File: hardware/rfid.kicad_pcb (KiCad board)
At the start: 2 copper layers, 75 x 50 mm, 34 parts, among them P1 CONN_01X02, P2 COMMS, U1 CR95HF

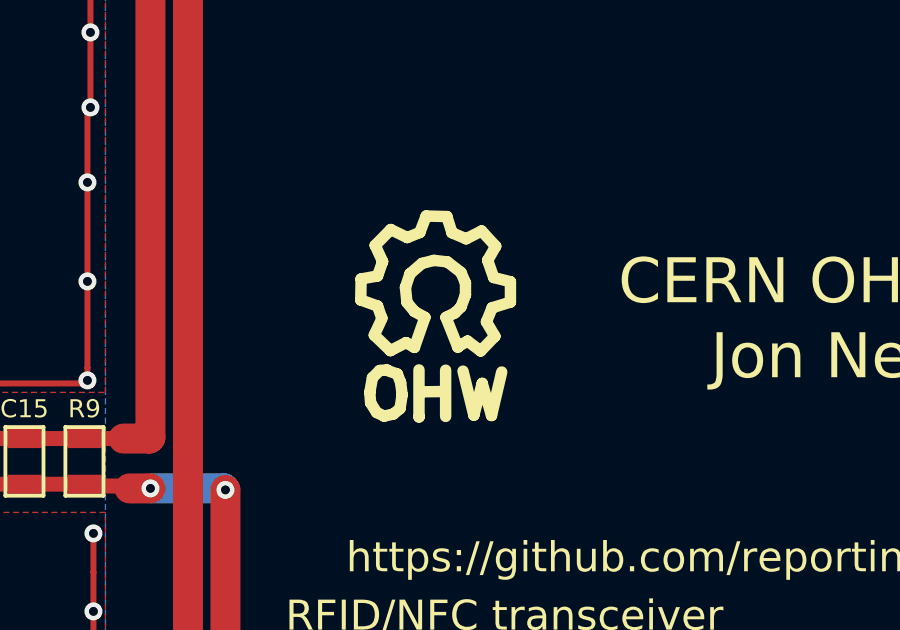
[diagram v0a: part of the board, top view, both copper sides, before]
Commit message: Thought that the correct phrase was OHW when it is actually OSHW. Updated board and gerbers to reflect this.
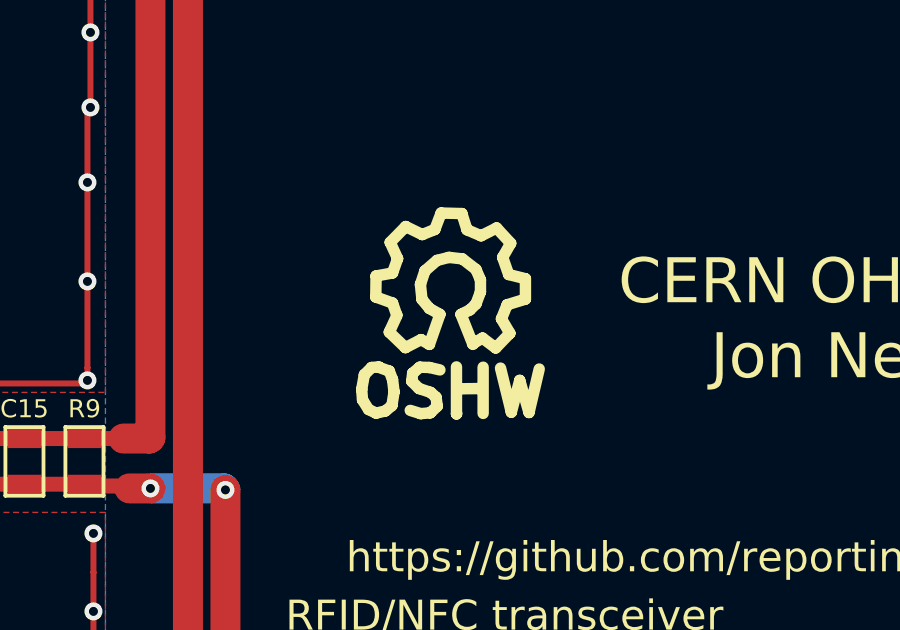
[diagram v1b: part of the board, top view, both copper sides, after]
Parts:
- removed the SYM at (191.0, 79.6)
- added SYM: Symbol_OSHW-Logo_SilkScreen_07Jul2012, Symbols:Symbol_OSHW-Logo_SilkScreen, F.Cu at (191.5, 79.5)
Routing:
- net GND: vias 58 -> 57
- net (no net): vias 3 -> 4
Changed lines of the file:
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@@
     (visible_elements FFFEFF7F)
     (pcbplotparams
-      (layerselection 0x00030_80000001)
-      (usegerberextensions false)
+      (layerselection 0x010f0_80000001)
+      (usegerberextensions true)
+      (gerberprecision 5)
       (excludeedgelayer true)
       (linewidth 0.100000)
@@
       (psa4output false)
       (plotreference true)
-      (plotvalue true)
+      (plotvalue false)
       (plotinvisibletext false)
       (padsonsilk false)
@@
       (outputformat 1)
       (mirror false)
-      (drillshape 1)
+      (drillshape 0)
       (scaleselection 1)
-      (outputdirectory ""))
+      (outputdirectory gerbers/rfid/))
   )
   (net 0 "")
@@
       (net 34 "Net-(G1-Pad4)"))
   )
-  (module rfid:Symbol_OHW-Logo_SilkScreen (layer F.Cu)
-    (at 191 79.6)
+  (module Symbols:Symbol_OSHW-Logo_SilkScreen (layer F.Cu)
+    (at 191.5 79.5)
     (descr "Symbol, OSHW-Logo, Silk Screen,")
     (tags "Symbol, OSHW-Logo, Silk Screen,")
@@
       (effects (font (thickness 0.3048)))
     )
-    (fp_line (start 0.91878 2.68986) (end 1.27946 4.16052) (layer F.SilkS) (width 0.381))
-    (fp_line (start 1.27946 4.16052) (end 1.55886 3.0988) (layer F.SilkS) (width 0.381))
-    (fp_line (start 1.55886 3.0988) (end 1.86874 4.17068) (layer F.SilkS) (width 0.381))
-    (fp_line (start 1.86874 4.17068) (end 2.2091 2.72034) (layer F.SilkS) (width 0.381))
-    (fp_line (start -0.50108 3.38074) (end 0.28886 3.37058) (layer F.SilkS) (width 0.381))
-    (fp_line (start 0.28886 3.37058) (end 0.29902 3.38074) (layer F.SilkS) (width 0.381))
-    (fp_line (start 0.29902 3.38074) (end 0.29902 3.37058) (layer F.SilkS) (width 0.381))
-    (fp_line (start 0.33966 2.65938) (end 0.33966 4.20116) (layer F.SilkS) (width 0.381))
-    (fp_line (start -0.54934 2.64922) (end -0.54934 4.21894) (layer F.SilkS) (width 0.381))
-    (fp_line (start -0.54934 4.21894) (end -0.53918 4.20878) (layer F.SilkS) (width 0.381))
-    (fp_line (start -1.60998 2.64922) (end -1.8589 2.66954) (layer F.SilkS) (width 0.381))
-    (fp_line (start -1.8589 2.66954) (end -2.1002 2.91084) (layer F.SilkS) (width 0.381))
-    (fp_line (start -2.1002 2.91084) (end -2.1891 3.40106) (layer F.SilkS) (width 0.381))
-    (fp_line (start -2.1891 3.40106) (end -2.16116 3.74904) (layer F.SilkS) (width 0.381))
-    (fp_line (start -2.16116 3.74904) (end -1.9605 4.06908) (layer F.SilkS) (width 0.381))
-    (fp_line (start -1.9605 4.06908) (end -1.70904 4.191) (layer F.SilkS) (width 0.381))
-    (fp_line (start -1.70904 4.191) (end -1.39916 4.11988) (layer F.SilkS) (width 0.381))
-    (fp_line (start -1.39916 4.11988) (end -1.18072 3.93954) (layer F.SilkS) (width 0.381))
-    (fp_line (start -1.18072 3.93954) (end -1.1096 3.4798) (layer F.SilkS) (width 0.381))
-    (fp_line (start -1.1096 3.4798) (end -1.1604 3.07086) (layer F.SilkS) (width 0.381))
-    (fp_line (start -1.1604 3.07086) (end -1.26962 2.78892) (layer F.SilkS) (width 0.381))
-    (fp_line (start -1.26962 2.78892) (end -1.6303 2.65938) (layer F.SilkS) (width 0.381))
+    (fp_line (start 1.66878 2.68986) (end 2.02946 4.16052) (layer F.SilkS) (width 0.381))
+    (fp_line (start 2.02946 4.16052) (end 2.30886 3.0988) (layer F.SilkS) (width 0.381))
+    (fp_line (start 2.30886 3.0988) (end 2.61874 4.17068) (layer F.SilkS) (width 0.381))
+    (fp_line (start 2.61874 4.17068) (end 2.9591 2.72034) (layer F.SilkS) (width 0.381))
+    (fp_line (start 0.24892 3.38074) (end 1.03886 3.37058) (layer F.SilkS) (width 0.381))
+    (fp_line (start 1.03886 3.37058) (end 1.04902 3.38074) (layer F.SilkS) (width 0.381))
+    (fp_line (start 1.04902 3.38074) (end 1.04902 3.37058) (layer F.SilkS) (width 0.381))
+    (fp_line (start 1.08966 2.65938) (end 1.08966 4.20116) (layer F.SilkS) (width 0.381))
+    (fp_line (start 0.20066 2.64922) (end 0.20066 4.21894) (layer F.SilkS) (width 0.381))
+    (fp_line (start 0.20066 4.21894) (end 0.21082 4.20878) (layer F.SilkS) (width 0.381))
+    (fp_line (start -0.35052 2.75082) (end -0.70104 2.66954) (layer F.SilkS) (width 0.381))
+    (fp_line (start -0.70104 2.66954) (end -1.02108 2.65938) (layer F.SilkS) (width 0.381))
+    (fp_line (start -1.02108 2.65938) (end -1.25984 2.86004) (layer F.SilkS) (width 0.381))
+    (fp_line (start -1.25984 2.86004) (end -1.29032 3.12928) (layer F.SilkS) (width 0.381))
+    (fp_line (start -1.29032 3.12928) (end -1.04902 3.37058) (layer F.SilkS) (width 0.381))
+    (fp_line (start -1.04902 3.37058) (end -0.6604 3.50012) (layer F.SilkS) (width 0.381))
+    (fp_line (start -0.6604 3.50012) (end -0.48006 3.66014) (layer F.SilkS) (width 0.381))
+    (fp_line (start -0.48006 3.66014) (end -0.43942 3.95986) (layer F.SilkS) (width 0.381))
+    (fp_line (start -0.43942 3.95986) (end -0.67056 4.18084) (layer F.SilkS) (width 0.381))
+    (fp_line (start -0.67056 4.18084) (end -0.9906 4.20878) (layer F.SilkS) (width 0.381))
+    (fp_line (start -0.9906 4.20878) (end -1.34112 4.09956) (layer F.SilkS) (width 0.381))
+    (fp_line (start -2.37998 2.64922) (end -2.6289 2.66954) (layer F.SilkS) (width 0.381))
+    (fp_line (start -2.6289 2.66954) (end -2.8702 2.91084) (layer F.SilkS) (width 0.381))
+    (fp_line (start -2.8702 2.91084) (end -2.9591 3.40106) (layer F.SilkS) (width 0.381))
+    (fp_line (start -2.9591 3.40106) (end -2.93116 3.74904) (layer F.SilkS) (width 0.381))
+    (fp_line (start -2.93116 3.74904) (end -2.7305 4.06908) (layer F.SilkS) (width 0.381))
+    (fp_line (start -2.7305 4.06908) (end -2.47904 4.191) (layer F.SilkS) (width 0.381))
+    (fp_line (start -2.47904 4.191) (end -2.16916 4.11988) (layer F.SilkS) (width 0.381))
+    (fp_line (start -2.16916 4.11988) (end -1.95072 3.93954) (layer F.SilkS) (width 0.381))
+    (fp_line (start -1.95072 3.93954) (end -1.8796 3.4798) (layer F.SilkS) (width 0.381))
+    (fp_line (start -1.8796 3.4798) (end -1.9304 3.07086) (layer F.SilkS) (width 0.381))
+    (fp_line (start -1.9304 3.07086) (end -2.03962 2.78892) (layer F.SilkS) (width 0.381))
+    (fp_line (start -2.03962 2.78892) (end -2.4003 2.65938) (layer F.SilkS) (width 0.381))
     (fp_line (start -1.78054 0.92964) (end -2.03962 1.49098) (layer F.SilkS) (width 0.381))
     (fp_line (start -2.03962 1.49098) (end -1.50114 2.00914) (layer F.SilkS) (width 0.381))
@@
   (via (at 176 108.5) (size 0.6) (drill 0.3) (layers F.Cu B.Cu) (net 0))
   (via (at 175.9 82.5) (size 0.6) (drill 0.3) (layers F.Cu B.Cu) (net 0))
+  (via (at 179.5 106.3) (size 0.6) (drill 0.3) (layers F.Cu B.Cu) (net 0))
   (segment (start 162.7 89.4) (end 163.3 88.8) (width 0.15) (layer F.Cu) (net 1))
   (segment (start 163.3 88.8) (end 164 88.8) (width 0.15) (layer F.Cu) (net 1))
@@
   (segment (start 179.5 107) (end 179.5 105.5) (width 0.2) (layer F.Cu) (net 2))
   (segment (start 179.5 108.5) (end 179.5 107) (width 0.2) (layer F.Cu) (net 2))
-  (via (at 179.5 106.3) (size 0.6) (drill 0.3) (layers F.Cu B.Cu) (net 2))
   (segment (start 177 108.5) (end 179.5 108.5) (width 0.2) (layer F.Cu) (net 2))
   (via (at 179.5 108.5) (size 0.6) (drill 0.3) (layers F.Cu B.Cu) (net 2))
@@
     )
   )
-  (zone (net 2) (net_name GND) (layer F.SilkS) (hatch edge 0.508)
+  (zone (net 0) (net_name "") (layer F.SilkS) (hatch edge 0.508)
     (connect_pads (clearance 0.15))
     (min_thickness 0.15)

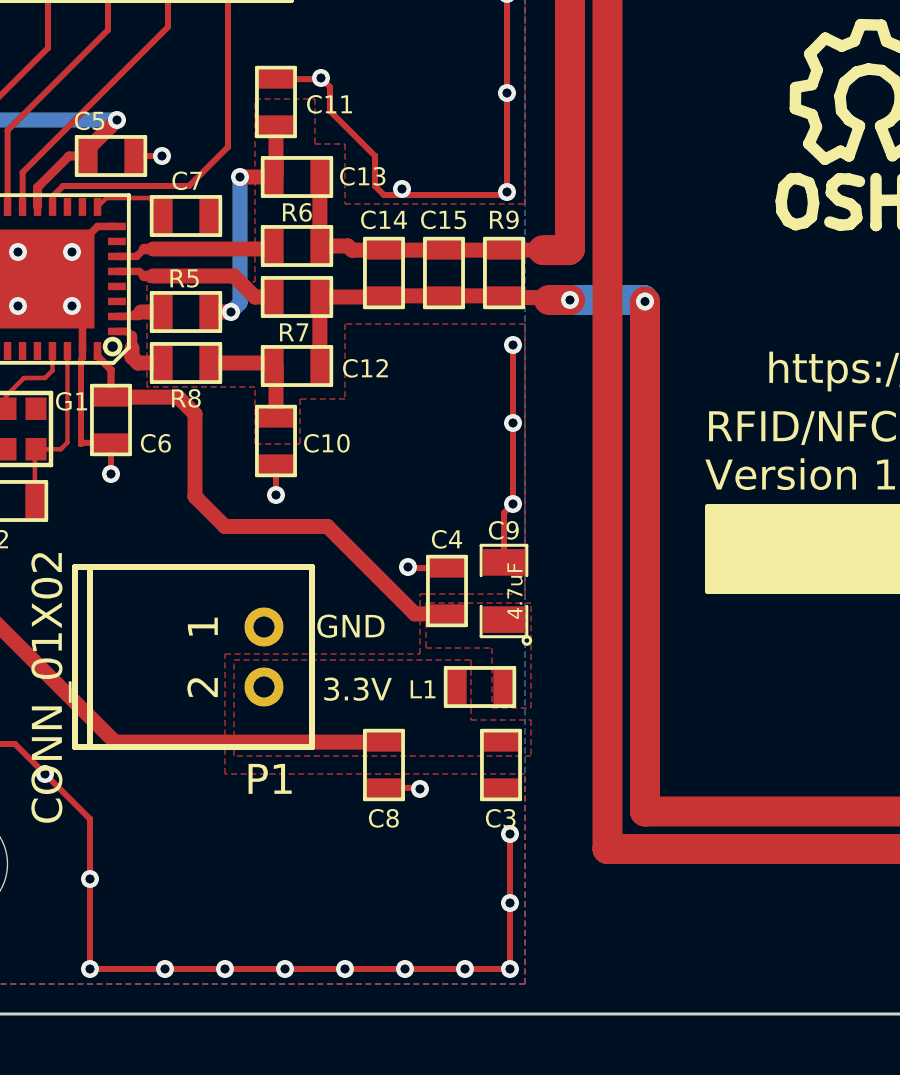
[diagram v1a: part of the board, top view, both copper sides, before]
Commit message: A few vias weren't connected to the ground net, fixed that. Also added a zipped up version of the gerbers that were sent to oshpark.
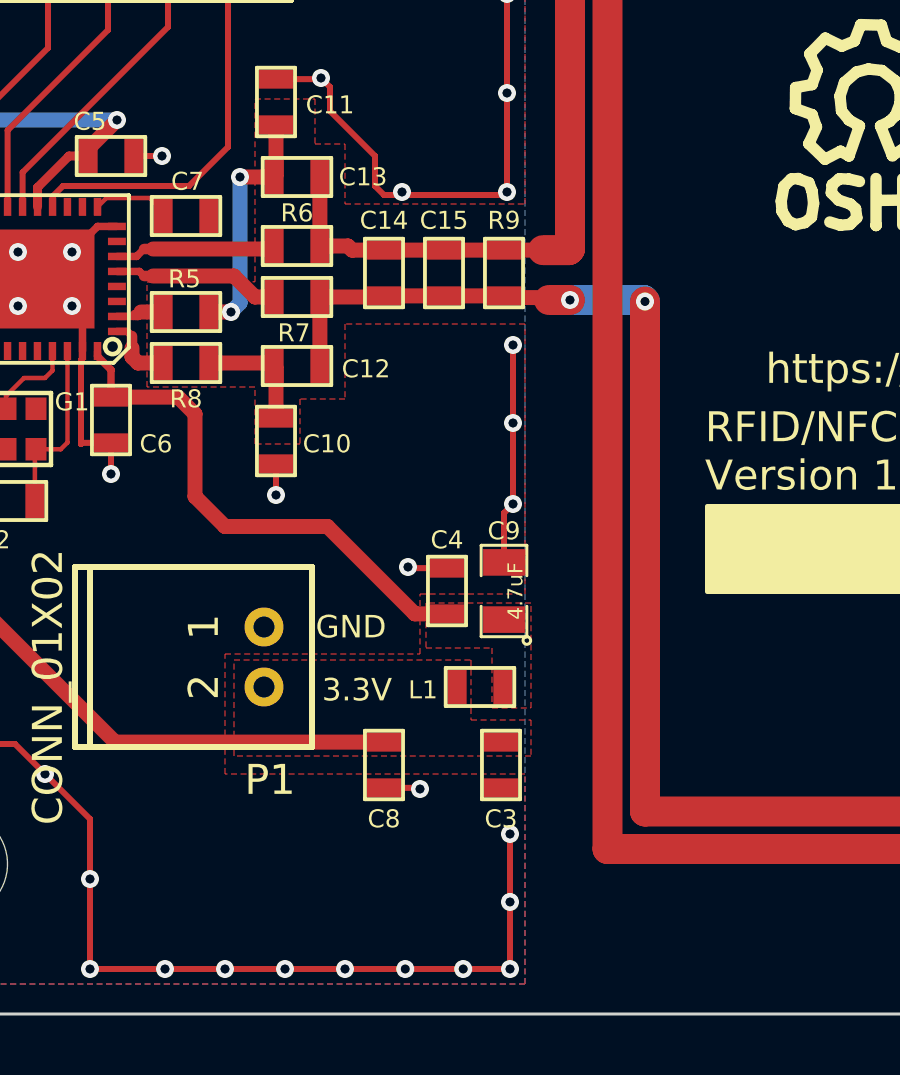
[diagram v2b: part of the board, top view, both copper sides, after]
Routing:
- net GND: track 156.2 -> 156.7 mm, vias 57 -> 61
- net (no net): vias 4 -> 0
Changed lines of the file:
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@@
 (kicad_pcb (version 4) (host pcbnew "(2014-09-17 BZR 5140)-product")
   (general
-    (links 0)
-    (no_connects 2)
+    (links 61)
+    (no_connects 0)
     (area 135.37017 59.926 251.62983 111.37046)
     (thickness 1.6)
     (drawings 14)
-    (tracks 297)
+    (tracks 306)
     (zones 0)
     (modules 34)
@@
   (layers
     (0 F.Cu signal)
-    (31 B.Cu signal hide)
+    (31 B.Cu signal)
     (32 B.Adhes user)
     (33 F.Adhes user)
@@
   (gr_line (start 231 65) (end 231 105) (angle 90) (layer Edge.Cuts) (width 0.1))
   (gr_line (start 161 60) (end 226 60) (angle 90) (layer Edge.Cuts) (width 0.1))
-  (via (at 178 108.5) (size 0.6) (drill 0.3) (layers F.Cu B.Cu) (net 0))
-  (via (at 176 108.5) (size 0.6) (drill 0.3) (layers F.Cu B.Cu) (net 0))
-  (via (at 175.9 82.5) (size 0.6) (drill 0.3) (layers F.Cu B.Cu) (net 0))
-  (via (at 179.5 106.3) (size 0.6) (drill 0.3) (layers F.Cu B.Cu) (net 0))
   (segment (start 162.7 89.4) (end 163.3 88.8) (width 0.15) (layer F.Cu) (net 1))
   (segment (start 163.3 88.8) (end 164 88.8) (width 0.15) (layer F.Cu) (net 1))
@@
   (segment (start 162.613 89.738) (end 162.7 89.825) (width 0.15) (layer F.Cu) (net 1))
   (segment (start 160.9 89.738) (end 162.613 89.738) (width 0.15) (layer F.Cu) (net 1))
+  (segment (start 175.926319 82.699999) (end 179.300001 82.699999) (width 0.2) (layer F.Cu) (net 2))
+  (segment (start 175.299999 82.699999) (end 175.926319 82.699999) (width 0.2) (layer F.Cu) (net 2))
+  (segment (start 175.926319 82.699999) (end 175.926319 82.626319) (width 0.2) (layer F.Cu) (net 2))
+  (segment (start 175.926319 82.626319) (end 175.9 82.6) (width 0.2) (layer F.Cu) (net 2))
+  (via (at 175.9 82.6) (size 0.6) (drill 0.3) (layers F.Cu B.Cu) (net 2))
+  (segment (start 179.5 106.525407) (end 179.5 105.5) (width 0.2) (layer F.Cu) (net 2))
+  (segment (start 179.5 107) (end 179.5 106.525407) (width 0.2) (layer F.Cu) (net 2))
+  (segment (start 179.5 106.525407) (end 179.5 106.265763) (width 0.2) (layer F.Cu) (net 2))
+  (via (at 179.5 106.265763) (size 0.6) (drill 0.3) (layers F.Cu B.Cu) (net 2))
+  (segment (start 177.808076 108.5) (end 179.5 108.5) (width 0.2) (layer F.Cu) (net 2))
+  (segment (start 177 108.5) (end 177.808076 108.5) (width 0.2) (layer F.Cu) (net 2))
+  (segment (start 177.808076 108.5) (end 177.940195 108.5) (width 0.2) (layer F.Cu) (net 2))
+  (via (at 177.940195 108.5) (size 0.6) (drill 0.3) (layers F.Cu B.Cu) (net 2))
+  (segment (start 176.028412 108.5) (end 177 108.5) (width 0.2) (layer F.Cu) (net 2))
+  (segment (start 175.5 108.5) (end 176.028412 108.5) (width 0.2) (layer F.Cu) (net 2))
+  (segment (start 176.028412 108.5) (end 176.008183 108.5) (width 0.2) (layer F.Cu) (net 2))
+  (via (at 176.008183 108.5) (size 0.6) (drill 0.3) (layers F.Cu B.Cu) (net 2))
   (segment (start 162.138 92.9) (end 160.9 92.9) (width 0.2) (layer F.Cu) (net 2))
   (via (at 160.9 92.9) (size 0.6) (drill 0.3) (layers F.Cu B.Cu) (net 2))
@@
   (segment (start 179.5 105.5) (end 179.5 104) (width 0.2) (layer F.Cu) (net 2))
   (via (at 179.5 104) (size 0.6) (drill 0.3) (layers F.Cu B.Cu) (net 2))
-  (segment (start 179.5 107) (end 179.5 105.5) (width 0.2) (layer F.Cu) (net 2))
   (segment (start 179.5 108.5) (end 179.5 107) (width 0.2) (layer F.Cu) (net 2))
-  (segment (start 177 108.5) (end 179.5 108.5) (width 0.2) (layer F.Cu) (net 2))
   (via (at 179.5 108.5) (size 0.6) (drill 0.3) (layers F.Cu B.Cu) (net 2))
-  (segment (start 175.5 108.5) (end 177 108.5) (width 0.2) (layer F.Cu) (net 2))
   (segment (start 174 108.5) (end 175.5 108.5) (width 0.2) (layer F.Cu) (net 2))
   (segment (start 172 108.5) (end 174 108.5) (width 0.2) (layer F.Cu) (net 2))
@@
   (via (at 179.4 79.3) (size 0.6) (drill 0.3) (layers F.Cu B.Cu) (net 2))
   (segment (start 175 82.4) (end 175.299999 82.699999) (width 0.2) (layer F.Cu) (net 2))
-  (segment (start 175.299999 82.699999) (end 179.300001 82.699999) (width 0.2) (layer F.Cu) (net 2))
   (segment (start 179.300001 82.699999) (end 179.4 82.6) (width 0.2) (layer F.Cu) (net 2))
   (via (at 179.4 82.6) (size 0.6) (drill 0.3) (layers F.Cu B.Cu) (net 2))
